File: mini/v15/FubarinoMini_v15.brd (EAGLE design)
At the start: 50.8 x 17.8 mm, 35 parts, among them IC1 MCP1702T-3302E/MB, J1 M20, J2 M20, Q1 8MHz, Q2 32.768 KHz, U1 PIC32MX250F128D_44VTLA_44

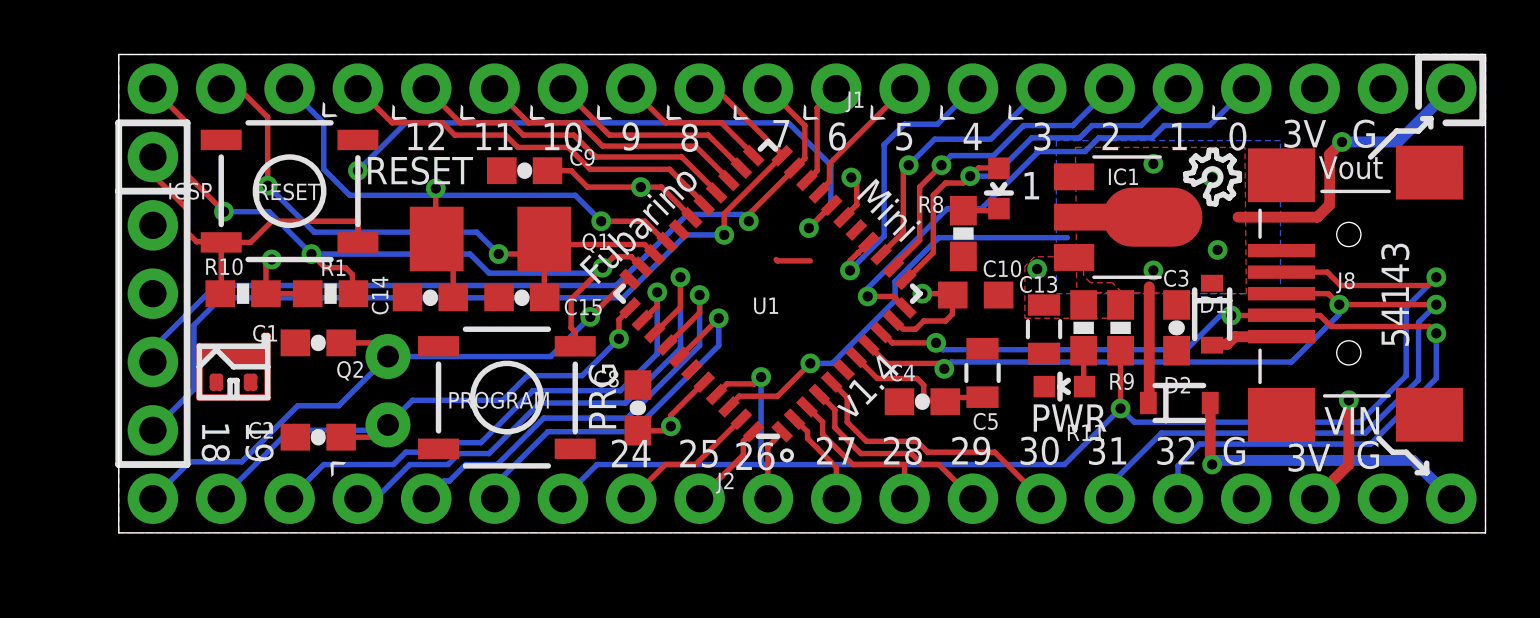
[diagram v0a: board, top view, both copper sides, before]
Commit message: Created first pass of assembly drawing, drill drawing, and BOM in Microchip format.
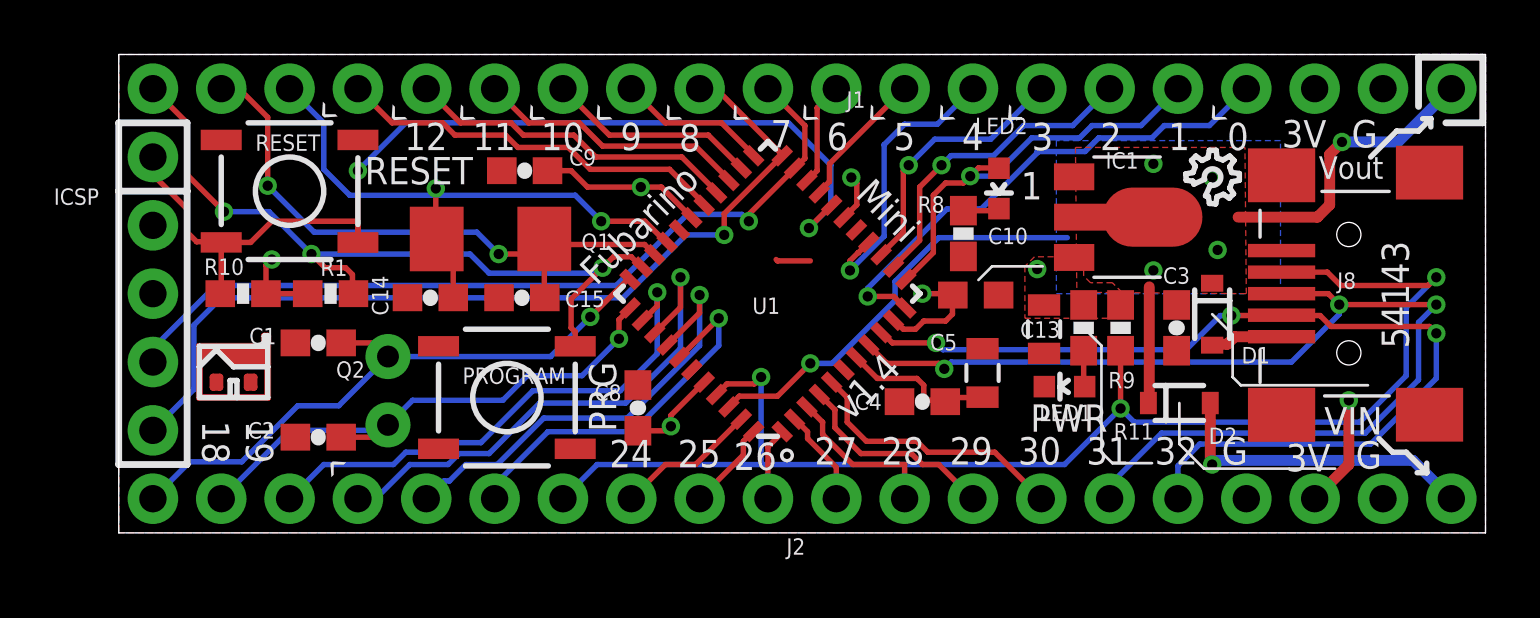
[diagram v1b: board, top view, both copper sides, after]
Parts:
- added DRILEGEND: (no value), drilegend:DRILEGEND
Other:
- board text added: "01-16"
- board text added: "01-20"
- board text added: "ASSEMBLY NOTES: UNLESS OTHERWISE SPECIFIED 1. ALL COMONENTS ARE RoHS COMPLIANT. 2. ALL THROUGH HOLE COMPONENTS MOUNTED ON THE TOP SIDE 3. ALL COMPONENTS AHLL BE MOUNTED FLUSH TO THE BOARD 4. ALL UNUSED COMPONENTS PADS SHALL BE FREE OF SOLDER 5. ALL LEADS SHALL BE TRIMMED TO A MAXIMUM LENGTH OF : N/A 6. MAXIMUM COMPONENT HEIGHT NOT TO EXEED: N/A 7. THESE COMPONENTS REQUIRE SOCKETS: NONE. 8. UNPOPU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"
- board text added: "LAYER-STACK"
- board text added: "Notes: This PCB to be manufactued to meet all acceptance levels of a CLASS 2 PCB per ANSI/IPC-A-600G. Material: Isola PCL370HR FR-4 or equivalent. Multilayer 2 Layers Controlled Impedance Cu weight external layers : 1oz Cu weight internal layers : Finished overall thickenss : 0.062 Finish: Immersion Gold X Immersion Tin Soldermask over bare copper (SMOBC) with Hot-Air-Leveled-Solder If edge conne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"
- board text added: "TITLE: FUBARINO MINI VERSION: 1.5 DATE: 2/24/2013 PCB DESIGNER: BRIAN SCHMALZ ENGINEER: BRIAN SCHMALZ"

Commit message: "final" version 1.5 files, submitted to Microchip for their approval Updated USB connector footprint to Microchip's fav Hirose
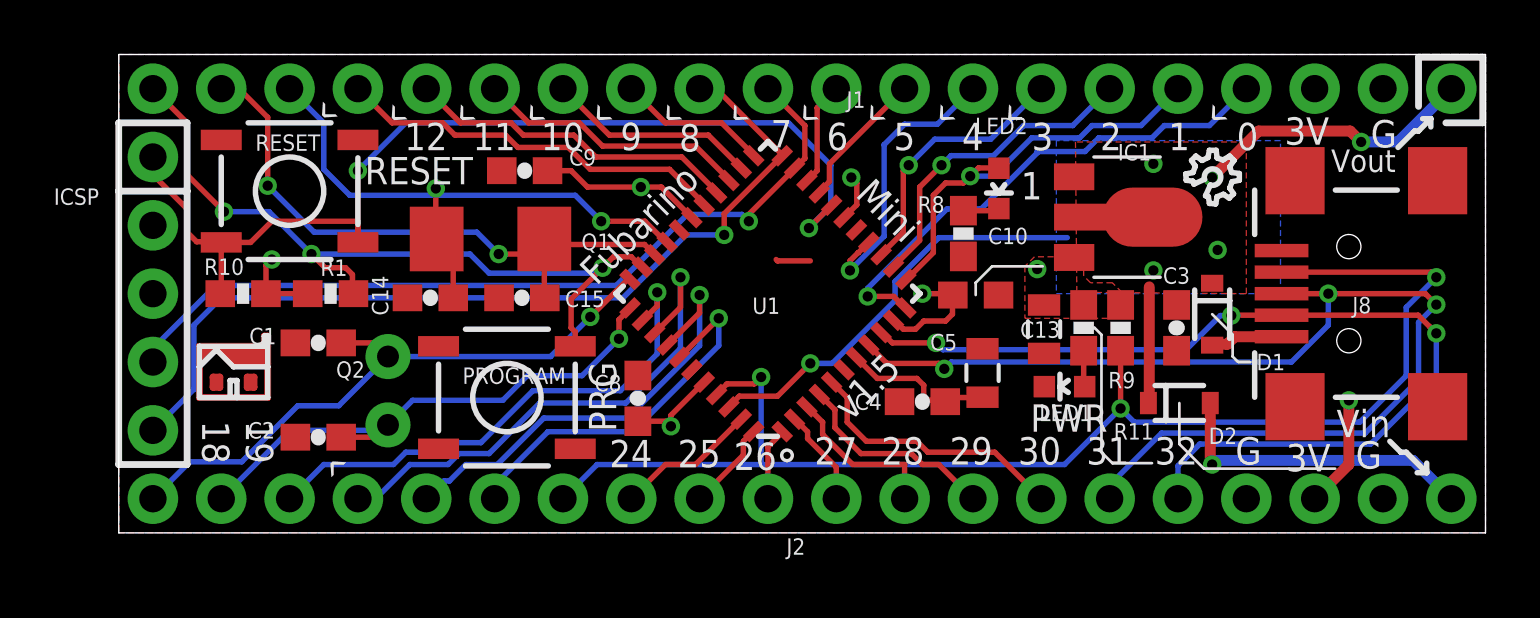
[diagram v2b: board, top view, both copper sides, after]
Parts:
- J8: value (none) -> USB-5PIN; device SparkFun02-20-08:USB-MINIB -> SchmalzHaus:USB-MINIB-5PIN-HIROSE-UX60-MB-5ST
- moved DRILEGEND 3.84 mm to (102.5, 30.2)
- moved U$2 0.68 mm to (45.9, 8.90)
- moved C8 0.36 mm to (19.3, 5.00)
- moved U$3 0.34 mm to (41.3, 6.49)
- turned J8 to 90 degrees
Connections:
- net GND: now also J8.MTN1, J8.MTN2, J8.MTN3, J8.MTN4; no longer J8.G1, J8.G2, J8.G3, J8.G4
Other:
- board text added: "v1.5"
- board text removed: "54143"
- board text removed: "VIN"
- board text removed: "v1.4"

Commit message: Updated Fubarino SD v1.5 board with CE, RoHS, chipKIT on silk, updated BOM, rendered top and bottom from gerbers.
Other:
- board text added: "Copyright 2012 Brian Schmalz Copyright and related rights are licensed under the Solderpad Hardware License, Version 0.51 (the “License”);"
- board text added: "See the License for the specific language governing permissions and limitations under the License."
- board text added: "software, hardware and materials distributed under this License is distributed on an “AS IS” BASIS, WITHOUT WARRANTIES OR CONDITIONS OF ANY KIND, either express or implied."
- board text added: "you may not use this file except in compliance with the License. You may obtain a copy of the License at http://solderpad.org/licenses/SHL-0.51. Unless required by applicable law or agreed to in writing,"
